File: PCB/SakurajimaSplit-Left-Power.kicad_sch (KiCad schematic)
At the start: 19 parts, among them J19 USB-C to Host, U4 TLV76733DRVR, U5 USBLC6-2SC6

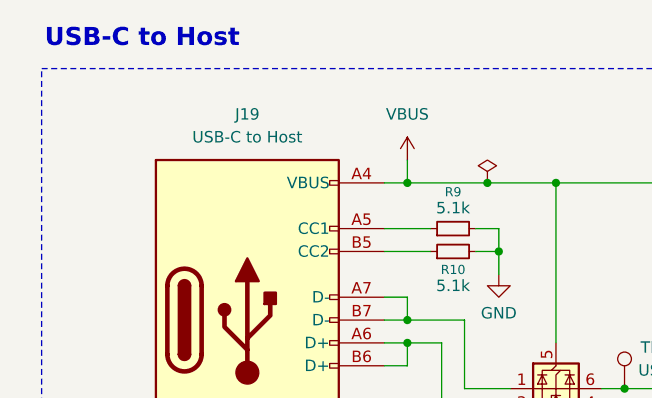
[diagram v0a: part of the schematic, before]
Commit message: feat(pcb): finish designing rough layout and update schematic
- Removed unused MCU pads
- Removed some GND testpoints
- Updated MCU connections based on PCB layout and MCU orientation
- Updated key matrix layout for a less aggressive one which feels more
  comfortable and more visually pleasing
- Re-annotated schematic
- Finished rough component placement
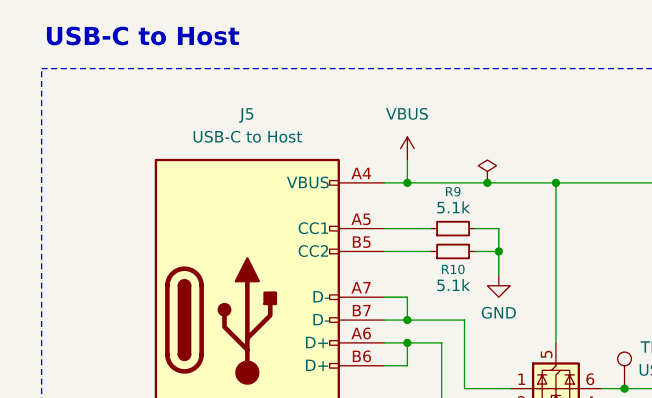
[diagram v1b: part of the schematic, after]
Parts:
- renumbered J19 to J5
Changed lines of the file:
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@@
+		(dnp no)
+		(fields_autoplaced yes)
+		(property "Reference" "#PWR024"
+			(at 226.06 152.4 0)
+			(effects
+				(font
+					(size 1.27 1.27)
+				)
+				(hide yes)
+			)
+		)
+		(property "Value" "GND"
+			(at 226.06 151.13 0)
+			(effects
+				(font
+					(size 1.27 1.27)
+				)
+			)
+		)
+		(property "Footprint" ""
+			(at 226.06 146.05 0)
+			(effects
+				(font
+					(size 1.27 1.27)
+					(thickness 0.254)
+					(bold yes)
+				)
+				(hide yes)
+			)
+		)
+		(property "Datasheet" ""
+			(at 226.06 146.05 0)
+			(effects
+				(font
+					(size 1.27 1.27)
+					(thickness 0.254)
+					(bold yes)
+				)
+				(hide yes)
+			)
+		)
+		(property "Description" "Power symbol creates a global label with name \"GND\" , ground"
+			(at 226.06 146.05 0)
+			(effects
+				(font
+					(size 1.27 1.27)
+					(thickness 0.254)
+					(bold yes)
+				)
+				(hide yes)
+			)
+		)
+		(pin "1"
+		)
+		(instances
+			(project "SakurajimaSplit"
+				(path "/2049b6de-7453-46e1-ab60-70116abff9d6/d08add9a-e5d5-49be-809e-a90adb11436d/38f7f4db-d52f-4e97-96ce-fcb5b455730e"
+					(reference "#PWR024")
+					(unit 1)
+				)
+			)
+		)
+	)
+	(symbol
+		(lib_id "power:GND")
+		(at 279.4 146.05 0)
+		(unit 1)
+		(exclude_from_sim no)
+		(in_bom yes)
+		(on_board yes)
 		(dnp no)
 		(fields_autoplaced yes)
 		(property "Reference" "#PWR026"
-			(at 226.06 152.4 0)
-			(effects
-				(font
-					(size 1.27 1.27)
-				)
-				(hide yes)
-			)
-		)
-		(property "Value" "GND"
-			(at 226.06 151.13 0)
-			(effects
-				(font
-					(size 1.27 1.27)
-				)
-			)
-		)
-		(property "Footprint" ""
-			(at 226.06 146.05 0)
-			(effects
-				(font
-					(size 1.27 1.27)
-					(thickness 0.254)
-					(bold yes)
-				)
-				(hide yes)
-			)
-		)
-		(property "Datasheet" ""
-			(at 226.06 146.05 0)
-			(effects
-				(font
-					(size 1.27 1.27)
-					(thickness 0.254)
-					(bold yes)
-				)
-				(hide yes)
-			)
-		)
-		(property "Description" "Power symbol creates a global label with name \"GND\" , ground"
-			(at 226.06 146.05 0)
-			(effects
-				(font
-					(size 1.27 1.27)
-					(thickness 0.254)
-					(bold yes)
-				)
-				(hide yes)
-			)
-		)
-		(pin "1"
-		)
-		(instances
-			(project "SakurajimaSplit"
-				(path "/2049b6de-7453-46e1-ab60-70116abff9d6/d08add9a-e5d5-49be-809e-a90adb11436d/38f7f4db-d52f-4e97-96ce-fcb5b455730e"
-					(reference "#PWR026")
-					(unit 1)
-				)
-			)
-		)
-	)
-	(symbol
-		(lib_id "power:GND")
-		(at 279.4 146.05 0)
-		(unit 1)
-		(exclude_from_sim no)
-		(in_bom yes)
-		(on_board yes)
-		(dnp no)
-		(fields_autoplaced yes)
-		(property "Reference" "#PWR028"
 			(at 279.4 152.4 0)
 			(effects
@@
 			(project "SakurajimaSplit"
 				(path "/2049b6de-7453-46e1-ab60-70116abff9d6/d08add9a-e5d5-49be-809e-a90adb11436d/38f7f4db-d52f-4e97-96ce-fcb5b455730e"
-					(reference "#PWR028")
+					(reference "#PWR026")
 					(unit 1)
 				)
@@
 		(dnp no)
 		(fields_autoplaced yes)
-		(property "Reference" "#PWR022"
+		(property "Reference" "#PWR020"
 			(at 147.32 120.65 0)
 			(effects
@@
 			(project "SakurajimaSplit"
 				(path "/2049b6de-7453-46e1-ab60-70116abff9d6/d08add9a-e5d5-49be-809e-a90adb11436d/38f7f4db-d52f-4e97-96ce-fcb5b455730e"
-					(reference "#PWR022")
+					(reference "#PWR020")
 					(unit 1)
 				)
@@
 		(dnp no)
 		(fields_autoplaced yes)
-		(property "Reference" "#PWR024"
+		(property "Reference" "#PWR022"
 			(at 242.57 134.62 0)
 			(effects
@@
 			(project "SakurajimaSplit"
 				(path "/2049b6de-7453-46e1-ab60-70116abff9d6/d08add9a-e5d5-49be-809e-a90adb11436d/38f7f4db-d52f-4e97-96ce-fcb5b455730e"
-					(reference "#PWR024")
+					(reference "#PWR022")
 					(unit 1)
 				)
@@
 		(dnp no)
 		(fields_autoplaced yes)
-		(property "Reference" "#PWR030"
+		(property "Reference" "#PWR028"
 			(at 163.83 158.75 0)
 			(effects
@@
 			(project "SakurajimaSplit"
 				(path "/2049b6de-7453-46e1-ab60-70116abff9d6/d08add9a-e5d5-49be-809e-a90adb11436d/38f7f4db-d52f-4e97-96ce-fcb5b455730e"
-					(reference "#PWR030")
+					(reference "#PWR028")
 					(unit 1)
 				)
@@
 		(dnp no)
 		(fields_autoplaced yes)
-		(property "Reference" "#PWR025"
+		(property "Reference" "#PWR023"
 			(at 327.66 134.62 0)
 			(effects
@@
 			(project "SakurajimaSplit"
 				(path "/2049b6de-7453-46e1-ab60-70116abff9d6/d08add9a-e5d5-49be-809e-a90adb11436d/38f7f4db-d52f-4e97-96ce-fcb5b455730e"
-					(reference "#PWR025")
+					(reference "#PWR023")
 					(unit 1)
 				)
@@
 		(dnp no)
 		(fields_autoplaced yes)
-		(property "Reference" "#PWR032"
+		(property "Reference" "#PWR030"
 			(at 129.54 168.91 0)
 			(effects
@@
 			(project "SakurajimaSplit"
 				(path "/2049b6de-7453-46e1-ab60-70116abff9d6/d08add9a-e5d5-49be-809e-a90adb11436d/38f7f4db-d52f-4e97-96ce-fcb5b455730e"
-					(reference "#PWR032")
+					(reference "#PWR030")
 					(unit 1)
 				)
@@
 		(dnp no)
 		(fields_autoplaced yes)
-		(property "Reference" "#PWR027"
+		(property "Reference" "#PWR025"
 			(at 246.38 152.4 0)
 			(effects
@@
 			(project "SakurajimaSplit"
 				(path "/2049b6de-7453-46e1-ab60-70116abff9d6/d08add9a-e5d5-49be-809e-a90adb11436d/38f7f4db-d52f-4e97-96ce-fcb5b455730e"
-					(reference "#PWR027")
+					(reference "#PWR025")
 					(unit 1)
 				)
@@
 		(on_board yes)
 		(dnp no)
-		(property "Reference" "#PWR023"
+		(property "Reference" "#PWR021"
 			(at 157.48 135.89 0)
 			(effects
@@
 			(project "SakurajimaSplit"
 				(path "/2049b6de-7453-46e1-ab60-70116abff9d6/d08add9a-e5d5-49be-809e-a90adb11436d/38f7f4db-d52f-4e97-96ce-fcb5b455730e"
-					(reference "#PWR023")
+					(reference "#PWR021")
 					(unit 1)
 				)
@@
 		(dnp no)
 		(fields_autoplaced yes)
-		(property "Reference" "J19"
+		(property "Reference" "J5"
 			(at 129.54 111.76 0)
 			(effects
@@
 			(project "SakurajimaSplit"
 				(path "/2049b6de-7453-46e1-ab60-70116abff9d6/d08add9a-e5d5-49be-809e-a90adb11436d/38f7f4db-d52f-4e97-96ce-fcb5b455730e"
-					(reference "J19")
+					(reference "J5")
 					(unit 1)
 				)
@@
 		(dnp no)
 		(fields_autoplaced yes)
-		(property "Reference" "#PWR031"
+		(property "Reference" "#PWR029"
 			(at 292.1 160.02 0)
 			(effects
@@
 			(project "SakurajimaSplit"
 				(path "/2049b6de-7453-46e1-ab60-70116abff9d6/d08add9a-e5d5-49be-809e-a90adb11436d/38f7f4db-d52f-4e97-96ce-fcb5b455730e"
-					(reference "#PWR031")
+					(reference "#PWR029")
 					(unit 1)
 				)
@@
 		(dnp no)
 		(fields_autoplaced yes)
-		(property "Reference" "#PWR029"
+		(property "Reference" "#PWR027"
 			(at 264.16 154.94 0)
 			(effects
@@
 			(project "SakurajimaSplit"
 				(path "/2049b6de-7453-46e1-ab60-70116abff9d6/d08add9a-e5d5-49be-809e-a90adb11436d/38f7f4db-d52f-4e97-96ce-fcb5b455730e"
-					(reference "#PWR029")
-					(unit 1)
-				)
+					(reference "#PWR027")
+					(unit 1)
+				)
